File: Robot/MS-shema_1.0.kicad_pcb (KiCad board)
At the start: 2 copper layers, 100 x 100 mm, 60 parts, among them M1 Motor Levi, M2 Motor Desni, P1 CONN_01X14, P2 CONN_01X14, Q1 Q_NPN_CBE, Q2 Q_PMOS_GSD, Q3 BSS138, Q4 BSS138, SW1 SWITCH_INV

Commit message: Add files via upload
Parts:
- BT1: footprint Robot:Battery -> Robot:BatteryHolder
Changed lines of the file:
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@@
     )
   )
-  (module Robot:Battery (layer F.Cu)
-    (at 160.528 110.744 180)
-    (fp_text reference BT1 (at 3.81 2.54 180) (layer F.SilkS)
-      (effects (font (size 1 1) (thickness 0.15)))
-    )
-    (fp_text value Baterija (at 3.81 -3.81 180) (layer F.Fab)
-      (effects (font (size 1 1) (thickness 0.15)))
-    )
-    (fp_line (start -2.87 0) (end -2.87 -53.85) (layer F.SilkS) (width 0.15))
-    (fp_line (start 26.7 0) (end 26.7 -53.85) (layer F.SilkS) (width 0.15))
-    (fp_line (start 20.83 0) (end 26.7 0) (layer F.SilkS) (width 0.15))
-    (fp_line (start -2.87 0) (end 3 0) (layer F.SilkS) (width 0.15))
-    (fp_line (start -2.87 -53.85) (end 26.7 -53.85) (layer F.SilkS) (width 0.15))
-    (pad 1 thru_hole oval (at 5.565 0 180) (size 4.5 2) (drill oval 3.5 1) (layers *.Cu *.Mask F.SilkS)
-      (net 1 +9V))
-    (pad 2 thru_hole oval (at 18.265 0 180) (size 4.5 2) (drill oval 3.5 1) (layers *.Cu *.Mask F.SilkS)
-      (net 2 GND))
-    (pad "" thru_hole circle (at 0 -15.24 180) (size 3.2 3.2) (drill 3) (layers *.Cu *.Mask F.SilkS))
-    (pad "" thru_hole circle (at 23.83 -15.24 180) (size 3.2 3.2) (drill 3) (layers *.Cu *.Mask F.SilkS))
-    (pad "" thru_hole circle (at 0 -37.47 180) (size 3.2 3.2) (drill 3) (layers *.Cu *.Mask F.SilkS))
-    (pad "" thru_hole circle (at 23.83 -37.47 180) (size 3.2 3.2) (drill 3) (layers *.Cu *.Mask F.SilkS))
-    (model ${KIPRJMOD}/3d/Battery.wrl
-      (at (xyz 1.25 -1.5 0.1))
-      (scale (xyz 0.393701 0.393701 0.393701))
-      (rotate (xyz 0 0 0))
-    )
-    (model ${KIPRJMOD}/3d/BatteryHolder.wrl
-      (at (xyz 0.465 1.03 0))
-      (scale (xyz 0.393701 0.393701 0.393701))
-      (rotate (xyz -90 0 90))
-    )
-  )
   (module Robot:RN42 (layer F.Cu)
     (at 176.276 120.396)
@@
     (pad ~ thru_hole circle (at 0 -20 180) (size 2.2 2.2) (drill 2.2) (layers *.Cu *.Mask))
   )
+  (module Robot:BatteryHolder (layer F.Cu)
+    (at 160.528 110.744 180)
+    (fp_text reference BT1 (at 3.81 2.54 180) (layer F.SilkS)
+      (effects (font (size 1 1) (thickness 0.15)))
+    )
+    (fp_text value Baterija (at 3.81 -3.81 180) (layer F.Fab)
+      (effects (font (size 1 1) (thickness 0.15)))
+    )
+    (fp_line (start 26.7 0) (end 26.8 -39.2) (layer F.SilkS) (width 0.15))
+    (fp_line (start 20.9 0) (end 26.7 0) (layer F.SilkS) (width 0.15))
+    (fp_line (start -2.8 0) (end -2.8 -39.3) (layer F.SilkS) (width 0.15))
+    (fp_line (start -2.8 0) (end 2.9 0) (layer F.SilkS) (width 0.15))
+    (pad 1 thru_hole oval (at 5.565 0 180) (size 4.5 2) (drill oval 3.5 1) (layers *.Cu *.Mask F.SilkS)
+      (net 1 +9V))
+    (pad 2 thru_hole oval (at 18.265 0 180) (size 4.5 2) (drill oval 3.5 1) (layers *.Cu *.Mask F.SilkS)
+      (net 2 GND))
+    (pad "" thru_hole circle (at 0 -15.24 180) (size 3.2 3.2) (drill 3) (layers *.Cu *.Mask F.SilkS))
+    (pad "" thru_hole circle (at 23.83 -15.24 180) (size 3.2 3.2) (drill 3) (layers *.Cu *.Mask F.SilkS))
+    (pad "" thru_hole circle (at 0 -37.47 180) (size 3.2 3.2) (drill 3) (layers *.Cu *.Mask F.SilkS))
+    (pad "" thru_hole circle (at 23.83 -37.47 180) (size 3.2 3.2) (drill 3) (layers *.Cu *.Mask F.SilkS))
+    (model ${KIPRJMOD}/3d/Battery.wrl
+      (at (xyz 1.25 -1.5 0.1))
+      (scale (xyz 0.393701 0.393701 0.393701))
+      (rotate (xyz 0 0 0))
+    )
+    (model ${KIPRJMOD}/3d/BatteryHolder.wrl
+      (at (xyz 0.465 1.03 0))
+      (scale (xyz 0.393701 0.393701 0.393701))
+      (rotate (xyz -90 0 90))
+    )
+  )
   (gr_arc (start 148.5011 209.0036) (end 170.306716 75.269666) (angle -9.26071) (layer Edge.Cuts) (width 0.1))

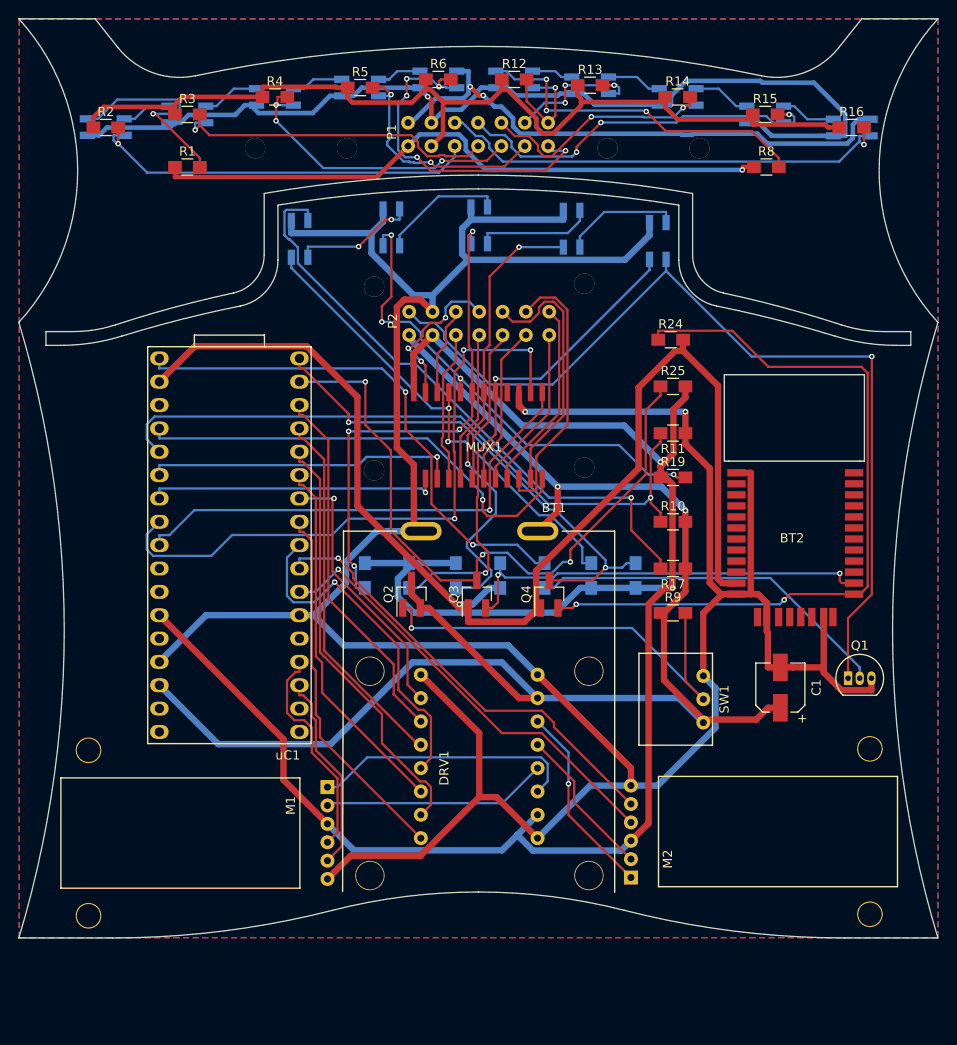
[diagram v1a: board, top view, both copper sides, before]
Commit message: Spremenjena je velikost PCB vezja
Sedaj je celoten PCB znotraj 100x100 mm (spremenjena obroba edge cuts - zamenjava z boss4)
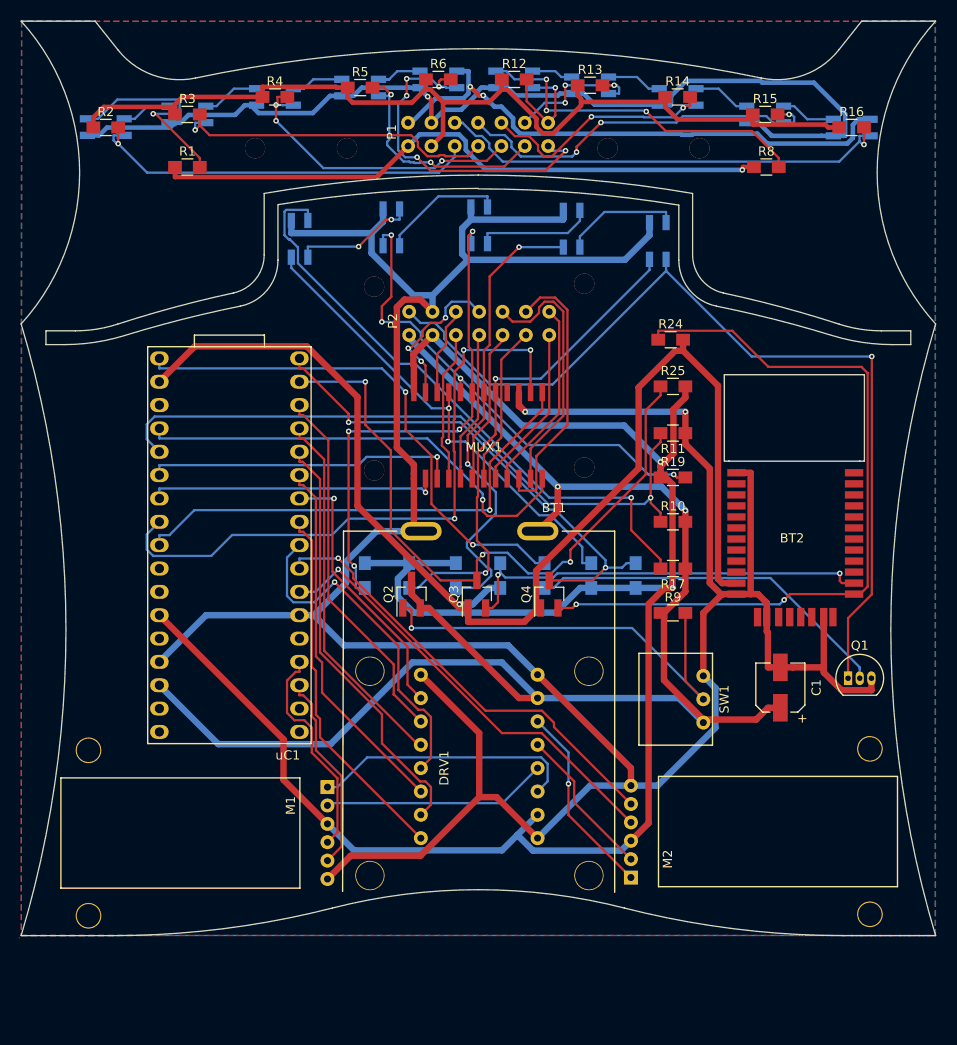
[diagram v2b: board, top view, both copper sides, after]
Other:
- board size 100 x 100 mm -> 99.5 x 99.5 mm
